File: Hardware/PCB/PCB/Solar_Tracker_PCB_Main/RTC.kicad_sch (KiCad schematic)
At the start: 1 part, among them IC4 PCF2131TFY

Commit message: Actualizacion PCB Principal
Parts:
- added BT1: 3.3, symbol Device:Battery_Cell
- added C12, C14: 100n, symbol Device:C
- added C15: Csup, symbol Device:C_Polarized
- added R11: Rsup, symbol Device:R
- added R12, R13, R14, R15: 10k, symbol Device:R
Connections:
- net VDD: now reaches IC4.1 (IFS)
- net VDD: now also R11.1, R12.1, R13.1, R14.1, R15.1
- net RTC_INTB: now reaches IC4.12 (~{INTB})
- net RTC_INTB: now also R14.2
- net RTC_INTA: now reaches IC4.13 (~{INTA})
- net RTC_INTA: now also R15.2
- net VDD_IN: now reaches IC4.15 (VDD)
- net VDD_IN: now also C14.2, C15.1, R11.2
- net VBAT: now reaches IC4.16 (VBAT)
- net VBAT: now also BT1.2 (-), C12.2
- net RTC_SCL: now reaches IC4.2 (SCL)
- net RTC_SCL: now also R12.2
- net GND: now reaches IC4.3 (SDI)
- net GND: now also IC4.4 (SDO), IC4.7 (VSS), BT1.1 (+), C12.1, C14.1, C15.2
- net RTC_SDA: now reaches IC4.5 (SDA/~{CE})
- net RTC_SDA: now also R13.2
- no-connect marks 0 -> 7
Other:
- moved on the sheet: IC4

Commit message: actualizacion pcb principal
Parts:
- C15: value Csup -> 1u
- R16: renamed from R11; value Rsup -> 47k
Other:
- note added: "Csup: Electrolytic capacitor"
- moved on the sheet: C14, C15, R16
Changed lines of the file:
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@@
+		)
+	)
+	(text "Csup: Electrolytic capacitor"
+		(exclude_from_sim no)
+		(at 27.432 43.688 0)
+		(effects
+			(font
+				(size 1.27 1.27)
+			)
 		)
 	)
@@
 	)
 	(junction
-		(at 29.21 30.48)
+		(at 30.48 27.94)
 		(diameter 0)
 		(color 0 0 0 0)
@@
 	(wire
 		(pts
-			(xy 33.02 22.86) (xy 29.21 22.86)
-		)
-		(stroke
-			(width 0)
-			(type default)
-		)
-	)
-	(wire
-		(pts
-			(xy 34.29 39.37) (xy 29.21 39.37)
-		)
-		(stroke
-			(width 0)
-			(type default)
-		)
-	)
-	(wire
-		(pts
-			(xy 33.02 30.48) (xy 29.21 30.48)
+			(xy 34.29 20.32) (xy 30.48 20.32)
+		)
+		(stroke
+			(width 0)
+			(type default)
+		)
+	)
+	(wire
+		(pts
+			(xy 35.56 36.83) (xy 30.48 36.83)
+		)
+		(stroke
+			(width 0)
+			(type default)
+		)
+	)
+	(wire
+		(pts
+			(xy 34.29 27.94) (xy 30.48 27.94)
 		)
 		(stroke
@@
 	(wire
 		(pts
-			(xy 26.67 30.48) (xy 29.21 30.48)
+			(xy 27.94 27.94) (xy 30.48 27.94)
 		)
 		(stroke
@@
 	(wire
 		(pts
-			(xy 29.21 39.37) (xy 29.21 30.48)
+			(xy 30.48 36.83) (xy 30.48 27.94)
 		)
 		(stroke
@@
 	(wire
 		(pts
-			(xy 29.21 22.86) (xy 29.21 30.48)
+			(xy 30.48 20.32) (xy 30.48 27.94)
 		)
 		(stroke
@@
 	(wire
 		(pts
-			(xy 41.91 39.37) (xy 45.72 39.37)
+			(xy 43.18 36.83) (xy 46.99 36.83)
 		)
 		(stroke
@@
 	)
 	(label "VDD_IN"
-		(at 26.67 30.48 180)
+		(at 27.94 27.94 180)
 		(effects
 			(font
@@
 	(symbol
 		(lib_id "power:VDD")
-		(at 45.72 39.37 270)
+		(at 46.99 36.83 270)
 		(unit 1)
 		(exclude_from_sim no)
@@
 		(fields_autoplaced yes)
 		(property "Reference" "#PWR022"
-			(at 41.91 39.37 0)
+			(at 43.18 36.83 0)
 			(effects
 				(font
@@
 		)
 		(property "Value" "VDD"
-			(at 50.8 39.37 0)
+			(at 52.07 36.83 0)
 			(effects
 				(font
@@
 		)
 		(property "Footprint" ""
-			(at 45.72 39.37 0)
+			(at 46.99 36.83 0)
 			(effects
 				(font
@@
 		)
 		(property "Datasheet" ""
-			(at 45.72 39.37 0)
+			(at 46.99 36.83 0)
 			(effects
 				(font
@@
 		)
 		(property "Description" "Power symbol creates a global label with name \"VDD\""
-			(at 45.72 39.37 0)
+			(at 46.99 36.83 0)
 			(effects
 				(font
@@
 	(symbol
 		(lib_id "Device:R")
-		(at 38.1 39.37 270)
+		(at 39.37 36.83 270)
 		(unit 1)
 		(exclude_from_sim no)
@@
 		(on_board yes)
 		(dnp no)
-		(property "Reference" "R11"
-			(at 36.576 43.942 90)
+		(property "Reference" "R16"
+			(at 37.846 41.402 90)
 			(effects
 				(font
@@
 			)
 		)
-		(property "Value" "Rsup"
-			(at 35.814 42.164 90)
+		(property "Value" "47k"
+			(at 37.084 39.624 90)
 			(effects
 				(font
@@
 		)
 		(property "Footprint" ""
-			(at 38.1 37.592 90)
+			(at 39.37 35.052 90)
 			(effects
 				(font
@@
 		)
 		(property "Datasheet" "~"
-			(at 38.1 39.37 0)
+			(at 39.37 36.83 0)
 			(effects
 				(font
@@
 		)
 		(property "Description" "Resistor"
-			(at 38.1 39.37 0)
+			(at 39.37 36.83 0)
 			(effects
 				(font
@@
 			(project "Solar_Tracker_PCB_Main"
 				(path "/99b6ddd9-7ffe-4c85-972a-e0f594a166d4/f065d8bf-f34b-491d-8721-3ae145af2fae"
-					(reference "R11")
+					(reference "R16")
 					(unit 1)
 				)
@@
 	(symbol
 		(lib_id "Device:C_Polarized")
-		(at 36.83 30.48 90)
+		(at 38.1 27.94 90)
 		(unit 1)
 		(exclude_from_sim no)
@@
 		(dnp no)
 		(property "Reference" "C15"
-			(at 35.56 36.576 90)
+			(at 36.83 34.036 90)
 			(effects
 				(font
@@
 			)
 		)
-		(property "Value" "Csup"
-			(at 35.052 34.29 90)
+		(property "Value" "1u"
+			(at 36.322 31.75 90)
 			(effects
 				(font
@@
 		)
 		(property "Footprint" ""
-			(at 40.64 29.5148 0)
+			(at 41.91 26.9748 0)
 			(effects
 				(font
@@
 		)
 		(property "Datasheet" "~"
-			(at 36.83 30.48 0)
+			(at 38.1 27.94 0)
 			(effects
 				(font
@@
 		)
 		(property "Description" "Polarized capacitor"
-			(at 36.83 30.48 0)
+			(at 38.1 27.94 0)
 			(effects
 				(font
@@
 	(symbol
 		(lib_id "power:GND")
-		(at 40.64 30.48 90)
+		(at 41.91 27.94 90)
 		(unit 1)
 		(exclude_from_sim no)
@@
 		(fields_autoplaced yes)
 		(property "Reference" "#PWR024"
-			(at 46.99 30.48 0)
+			(at 48.26 27.94 0)
 			(effects
 				(font
@@
 		)
 		(property "Value" "GND"
-			(at 45.72 30.48 0)
+			(at 46.99 27.94 0)
 			(effects
 				(font
@@
 		)
 		(property "Footprint" ""
-			(at 40.64 30.48 0)
+			(at 41.91 27.94 0)
 			(effects
 				(font
@@
 		)
 		(property "Datasheet" ""
-			(at 40.64 30.48 0)
+			(at 41.91 27.94 0)
 			(effects
 				(font
@@
 		)
 		(property "Description" "Power symbol creates a global label with name \"GND\" , ground"
-			(at 40.64 30.48 0)
+			(at 41.91 27.94 0)
 			(effects
 				(font
@@
 	(symbol
 		(lib_id "Device:C")
-		(at 36.83 22.86 270)
+		(at 38.1 20.32 270)
 		(unit 1)
 		(exclude_from_sim no)
@@
 		(dnp no)
 		(property "Reference" "C14"
-			(at 35.052 19.304 90)
+			(at 36.322 16.764 90)
 			(effects
 				(font
@@
 		)
 		(property "Value" "100n"
-			(at 34.798 17.018 90)
+			(at 36.068 14.478 90)
 			(effects
 				(font
@@
 		)
 		(property "Footprint" ""
-			(at 33.02 23.8252 0)
+			(at 34.29 21.2852 0)
 			(effects
 				(font
@@
 		)
 		(property "Datasheet" "~"
-			(at 36.83 22.86 0)
+			(at 38.1 20.32 0)
 			(effects
 				(font
@@
 		)
 		(property "Description" "Unpolarized capacitor"
-			(at 36.83 22.86 0)
+			(at 38.1 20.32 0)
 			(effects
 				(font
@@
 	(symbol
 		(lib_id "power:GND")
-		(at 40.64 22.86 90)
+		(at 41.91 20.32 90)
 		(unit 1)
 		(exclude_from_sim no)
@@
 		(fields_autoplaced yes)
 		(property "Reference" "#PWR023"
-			(at 46.99 22.86 0)
+			(at 48.26 20.32 0)
 			(effects
 				(font
@@
 		)
 		(property "Value" "GND"
-			(at 45.72 22.86 0)
+			(at 46.99 20.32 0)
 			(effects
 				(font
@@
 		)
 		(property "Footprint" ""
-			(at 40.64 22.86 0)
+			(at 41.91 20.32 0)
 			(effects
 				(font
@@
 		)
 		(property "Datasheet" ""
-			(at 40.64 22.86 0)
+			(at 41.91 20.32 0)
 			(effects
 				(font
@@
 		)
 		(property "Description" "Power symbol creates a global label with name \"GND\" , ground"
-			(at 40.64 22.86 0)
-			(effects
-				(font
+			(at 41.91 20.32 0)
+			(effects
+				(font

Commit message: Actualizacion de Footprints Resistencias y Capacitores Main PCB
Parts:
- C12, C14, C15: footprint (none) -> Capacitor_SMD:C_0805_2012Metric_Pad1.18x1.45mm_HandSolder
- R12, R13, R14, R15, R16: footprint (none) -> Resistor_SMD:R_0805_2012Metric_Pad1.20x1.40mm_HandSolder
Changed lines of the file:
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@@
 			)
 		)
-		(property "Footprint" ""
+		(property "Footprint" "Resistor_SMD:R_0805_2012Metric_Pad1.20x1.40mm_HandSolder"
 			(at 111.252 26.67 90)
 			(effects
@@
 			)
 		)
-		(property "Footprint" ""
+		(property "Footprint" "Resistor_SMD:R_0805_2012Metric_Pad1.20x1.40mm_HandSolder"
 			(at 136.652 26.67 90)
 			(effects
@@
 			)
 		)
-		(property "Footprint" ""
+		(property "Footprint" "Resistor_SMD:R_0805_2012Metric_Pad1.20x1.40mm_HandSolder"
 			(at 129.032 26.67 90)
 			(effects
@@
 			)
 		)
-		(property "Footprint" ""
+		(property "Footprint" "Resistor_SMD:R_0805_2012Metric_Pad1.20x1.40mm_HandSolder"
 			(at 39.37 35.052 90)
 			(effects
@@
 			)
 		)
-		(property "Footprint" ""
+		(property "Footprint" "Capacitor_SMD:C_0805_2012Metric_Pad1.18x1.45mm_HandSolder"
 			(at 41.91 26.9748 0)
 			(effects
@@
 			)
 		)
-		(property "Footprint" ""
+		(property "Footprint" "Resistor_SMD:R_0805_2012Metric_Pad1.20x1.40mm_HandSolder"
 			(at 120.142 26.67 90)
 			(effects
@@
 			)
 		)
-		(property "Footprint" ""
+		(property "Footprint" "Capacitor_SMD:C_0805_2012Metric_Pad1.18x1.45mm_HandSolder"
 			(at 72.6948 22.86 0)
 			(effects
@@
 			)
 		)
-		(property "Footprint" ""
+		(property "Footprint" "Capacitor_SMD:C_0805_2012Metric_Pad1.18x1.45mm_HandSolder"
 			(at 34.29 21.2852 0)
 			(effects

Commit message: Actualizacion de PCB Main
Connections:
- net GND: now also BT1.2 (-); no longer BT1.1 (+)
- net VBAT: now also BT1.1 (+); no longer BT1.2 (-)
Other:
- moved on the sheet: BT1
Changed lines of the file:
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@@
-	(wire
-		(pts
-			(xy 85.09 22.86) (xy 85.09 17.78)
-		)
-		(stroke
-			(width 0)
-			(type default)
-		)
-	)
 	(wire
 		(pts
@@
 		(pts
 			(xy 121.92 40.64) (xy 149.86 40.64)
+		)
+		(stroke
+			(width 0)
+			(type default)
+		)
+	)
+	(wire
+		(pts
+			(xy 85.09 17.78) (xy 85.09 22.86)
 		)
 		(stroke
@@
 	(symbol
 		(lib_id "Device:Battery_Cell")
-		(at 85.09 25.4 180)
+		(at 85.09 27.94 0)
 		(unit 1)
 		(exclude_from_sim no)
@@
 		(fields_autoplaced yes)
 		(property "Reference" "BT1"
-			(at 88.9 25.9714 0)
-			(effects
-				(font
-					(size 1.27 1.27)
-				)
-				(justify right)
+			(at 88.9 24.8284 0)
+			(effects
+				(font
+					(size 1.27 1.27)
+				)
+				(justify left)
 			)
 		)
 		(property "Value" "3.3"
-			(at 88.9 28.5114 0)
-			(effects
-				(font
-					(size 1.27 1.27)
-				)
-				(justify right)
+			(at 88.9 27.3684 0)
+			(effects
+				(font
+					(size 1.27 1.27)
+				)
+				(justify left)
 			)
 		)
 		(property "Footprint" ""
-			(at 85.09 26.924 90)
+			(at 85.09 26.416 90)
 			(effects
 				(font
@@
 		)
 		(property "Datasheet" "~"
-			(at 85.09 26.924 90)
+			(at 85.09 26.416 90)
 			(effects
 				(font
@@
 		)
 		(property "Description" "Single-cell battery"
-			(at 85.09 25.4 0)
+			(at 85.09 27.94 0)
 			(effects
 				(font
@@
 		)
 		(property "Sim.Device" "V"
-			(at 85.09 25.4 0)
+			(at 85.09 27.94 0)
 			(effects
 				(font
@@
 		)
 		(property "Sim.Type" "DC"
-			(at 85.09 25.4 0)
+			(at 85.09 27.94 0)
 			(effects
 				(font
@@
 		)
 		(property "Sim.Pins" "1=+ 2=-"
-			(at 85.09 25.4 0)
-			(effects
-				(font
+			(at 85.09 27.94 0)
+			(effects
+				(font

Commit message: Actualizacion Main pcb
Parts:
- removed BT1: 3.3, symbol Device:Battery_Cell
- added BT1: BAT-HLD-013-SMT-TR, BAT-HLD:BATHLD013SMTTR, symbol BAT-HLD-013-SMT-TR:BAT-HLD-013-SMT-TR
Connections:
- net GND: now also BT1.2 (-)
- net VBAT: now also BT1.1 (+)
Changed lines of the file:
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@@
 	(rectangle
 		(start 66.04 12.7)
-		(end 95.25 53.34)
+		(end 107.95 53.34)
 		(stroke
 			(width 0)
@@
 	)
 	(rectangle
-		(start 95.25 12.7)
+		(start 107.95 12.7)
 		(end 163.83 53.34)
 		(stroke
@@
 		(exclude_from_sim no)
 		(at 66.04 45.72 0)
-		(size 29.21 7.62)
+		(size 41.91 7.62)
 		(margins 0.9525 0.9525 0.9525 0.9525)
 		(stroke
@@
 	(text_box "RPU 10KΩ is recommended."
 		(exclude_from_sim no)
-		(at 95.25 45.72 0)
-		(size 68.58 7.62)
+		(at 107.95 45.72 0)
+		(size 55.88 7.62)
 		(margins 0.9525 0.9525 0.9525 0.9525)
 		(stroke
@@
 	(wire
 		(pts
-			(xy 85.09 30.48) (xy 85.09 34.29)
+			(xy 85.09 27.94) (xy 85.09 34.29)
 		)
 		(stroke
@@
 	(wire
 		(pts
+			(xy 86.36 27.94) (xy 85.09 27.94)
+		)
+		(stroke
+			(width 0)
+			(type default)
+		)
+	)
+	(wire
+		(pts
 			(xy 121.92 40.64) (xy 149.86 40.64)
 		)
@@
 	(wire
 		(pts
-			(xy 85.09 17.78) (xy 85.09 22.86)
-		)
-		(stroke
-			(width 0)
-			(type default)
-		)
-	)
-	(wire
-		(pts
 			(xy 130.81 22.86) (xy 130.81 21.59)
 		)
@@
 	(wire
 		(pts
+			(xy 85.09 17.78) (xy 85.09 25.4)
+		)
+		(stroke
+			(width 0)
+			(type default)
+		)
+	)
+	(wire
+		(pts
 			(xy 130.81 38.1) (xy 149.86 38.1)
 		)
@@
 		(pts
 			(xy 49.53 86.36) (xy 63.5 86.36)
+		)
+		(stroke
+			(width 0)
+			(type default)
+		)
+	)
+	(wire
+		(pts
+			(xy 86.36 25.4) (xy 85.09 25.4)
 		)
 		(stroke
@@
 	)
 	(symbol
+		(lib_id "BAT-HLD-013-SMT-TR:BAT-HLD-013-SMT-TR")
+		(at 86.36 25.4 0)
+		(unit 1)
+		(exclude_from_sim no)
+		(in_bom yes)
+		(on_board yes)
+		(dnp no)
+		(fields_autoplaced yes)
+		(property "Reference" "BT1"
+			(at 102.87 26.6699 0)
+			(effects
+				(font
+					(size 1.27 1.27)
+				)
+				(justify left)
+			)
+		)
+		(property "Value" "BAT-HLD-013-SMT-TR"
+			(at 102.87 27.9399 0)
+			(effects
+				(font
+					(size 1.27 1.27)
+				)
+				(justify left)
+				(hide yes)
+			)
+		)
+		(property "Footprint" "BAT-HLD:BATHLD013SMTTR"
+			(at 102.87 120.32 0)
+			(effects
+				(font
+					(size 1.27 1.27)
+				)
+				(justify left top)
+				(hide yes)
+			)
+		)
+		(property "Datasheet" "https://www.te.com/en/product-BAT-HLD-013-SMT-TR.html"
+			(at 102.87 220.32 0)
+			(effects
+				(font
+					(size 1.27 1.27)
+				)
+				(justify left top)
+				(hide yes)
+			)
+		)
+		(property "Description" "CR2032 Battery Holder, 1 Position, Horizontal, Nickel (Ni)"
+			(at 86.36 25.4 0)
+			(effects
+				(font
+					(size 1.27 1.27)
+				)
+				(hide yes)
+			)
+		)
+		(property "Height" "6.5"
+			(at 102.87 420.32 0)
+			(effects
+				(font
+					(size 1.27 1.27)
+				)
+				(justify left top)
+				(hide yes)
+			)
+		)
+		(property "Mouser Part Number" "712-BAT-HLD-013SMTTR"
+			(at 102.87 520.32 0)
+			(effects
+				(font
+					(size 1.27 1.27)
+				)
+				(justify left top)
+				(hide yes)
+			)
+		)
+		(property "Mouser Price/Stock" "https://www.mouser.co.uk/ProductDetail/TE-Connectivity-Linx-Technologies/BAT-HLD-013-SMT-TR?qs=4ASt3YYao0UKhYWrBts7tw%3D%3D"
+			(at 102.87 620.32 0)
+			(effects
+				(font
+					(size 1.27 1.27)
+				)
+				(justify left top)
+				(hide yes)
+			)
+		)
+		(property "Manufacturer_Name" "TE Connectivity"
+			(at 102.87 720.32 0)
+			(effects
+				(font
+					(size 1.27 1.27)
+				)
+				(justify left top)
+				(hide yes)
+			)
+		)
+		(property "Manufacturer_Part_Number" "BAT-HLD-013-SMT-TR"
+			(at 102.87 820.32 0)
+			(effects
+				(font
+					(size 1.27 1.27)
+				)
+				(justify left top)
+				(hide yes)
+			)
+		)
+		(pin "1"
+		)
+		(pin "2"
+		)
+		(instances
+			(project ""
+				(path "/99b6ddd9-7ffe-4c85-972a-e0f594a166d4/f065d8bf-f34b-491d-8721-3ae145af2fae"
+					(reference "BT1")
+					(unit 1)
+				)
+			)
+		)
+	)
+	(symbol
 		(lib_id "Device:R")
 		(at 113.03 26.67 0)
@@
 					(unit 1)
 				)
-			)
-		)
-	)
-	(symbol
-		(lib_id "Device:Battery_Cell")
-		(at 85.09 27.94 0)
-		(unit 1)
-		(exclude_from_sim no)
-		(in_bom yes)
-		(on_board yes)
-		(dnp no)
-		(fields_autoplaced yes)
-		(property "Reference" "BT1"
-			(at 88.9 24.8284 0)
-			(effects
-				(font
-					(size 1.27 1.27)
-				)
-				(justify left)
-			)
-		)
-		(property "Value" "3.3"
-			(at 88.9 27.3684 0)
-			(effects
-				(font
-					(size 1.27 1.27)
-				)
-				(justify left)
-			)
-		)
-		(property "Footprint" ""
-			(at 85.09 26.416 90)
-			(effects
-				(font
-					(size 1.27 1.27)
-				)
-				(hide yes)
-			)
-		)
-		(property "Datasheet" "~"
-			(at 85.09 26.416 90)
-			(effects
-				(font
-					(size 1.27 1.27)
-				)
-				(hide yes)
-			)
-		)
-		(property "Description" "Single-cell battery"
-			(at 85.09 27.94 0)
-			(effects
-				(font
-					(size 1.27 1.27)
-				)
-				(hide yes)
-			)
-		)
-		(property "Sim.Device" "V"
-			(at 85.09 27.94 0)
-			(effects
-				(font
-					(size 1.27 1.27)
-				)
-				(hide yes)
-			)
-		)
-		(property "Sim.Type" "DC"
-			(at 85.09 27.94 0)
-			(effects
-				(font
-					(size 1.27 1.27)
-				)
-				(hide yes)
-			)
-		)
-		(property "Sim.Pins" "1=+ 2=-"
-			(at 85.09 27.94 0)
-			(effects
-				(font
-					(size 1.27 1.27)
-				)
-				(hide yes)
-			)
-		)
-		(pin "2"
-		)
-		(pin "1"
-		)
-		(instances
-			(project ""
-				(path "/99b6ddd9-7ffe-4c85-972a-e0f594a166d4/f065d8bf-f34b-491d-8721-3ae145af2fae"
-					(reference "BT1")
-					(unit 1)
-				)

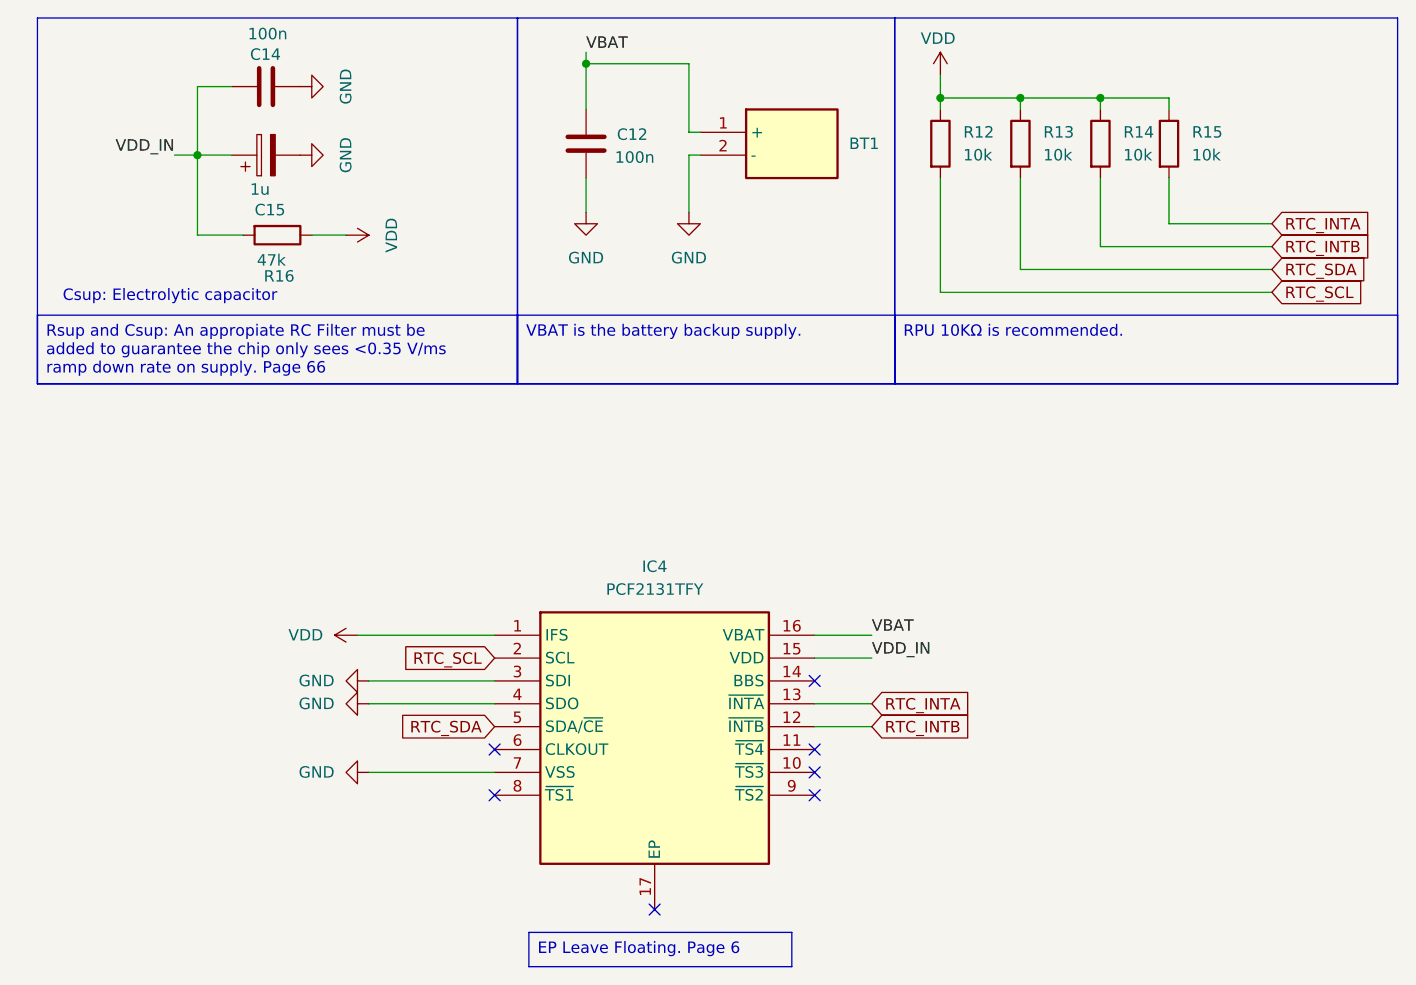
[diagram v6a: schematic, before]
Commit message: Modificaciones PCB MAIN
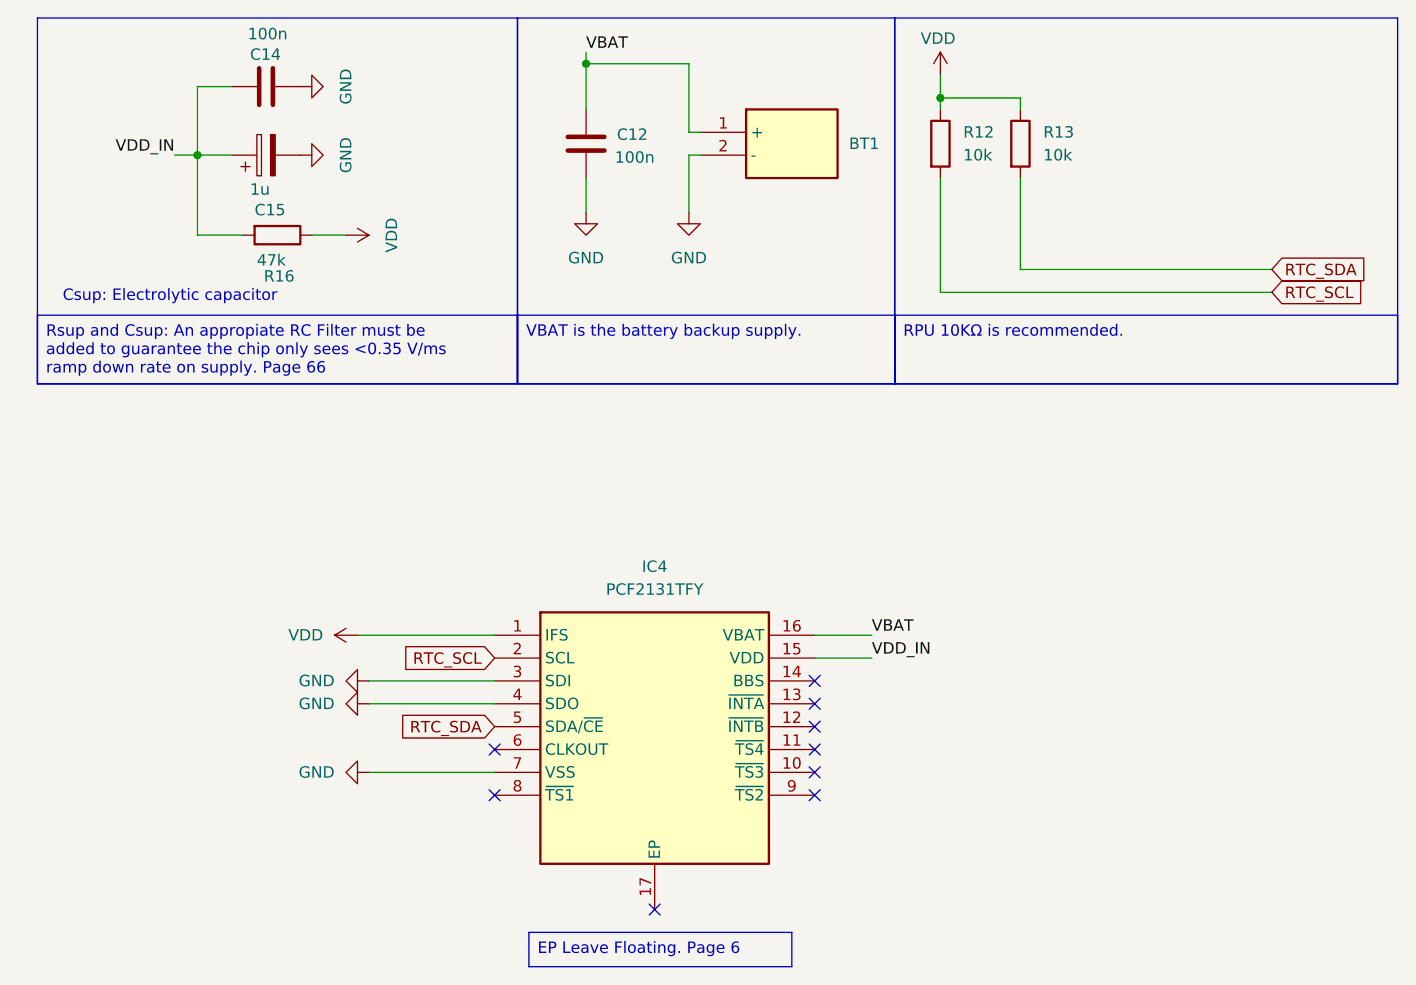
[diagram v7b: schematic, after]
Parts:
- removed R14, R15: 10k, Resistor_SMD:R_0805_2012Metric_Pad1.20x1.40mm_HandSolder, symbol Device:R
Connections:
- net RTC_INTA: no longer names the net of IC4.13 (~{INTA})
- net RTC_INTB: no longer names the net of IC4.12 (~{INTB})
- no-connect marks 7 -> 9
